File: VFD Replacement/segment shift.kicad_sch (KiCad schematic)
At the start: 28 parts, among them Q1 MMDT2222A

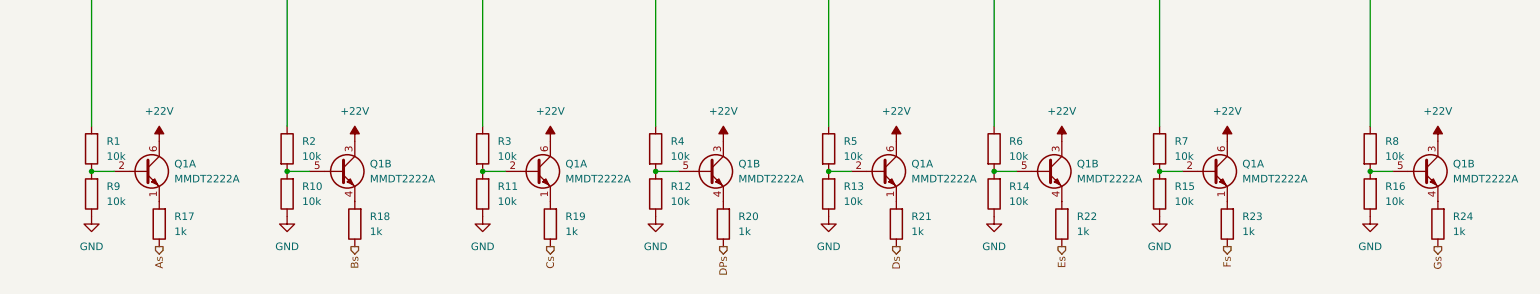
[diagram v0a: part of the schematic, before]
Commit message: Update VFD Replacement layout
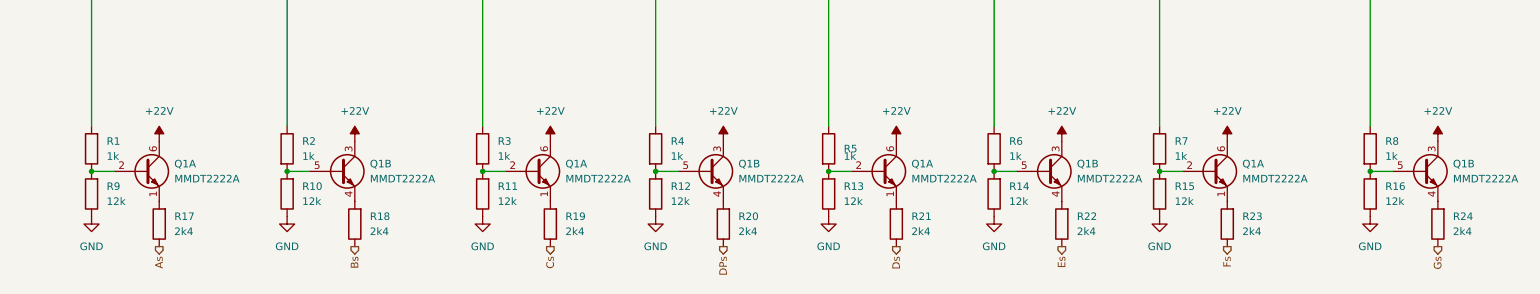
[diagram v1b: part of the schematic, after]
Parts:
- R1, R2, R3, R4, R5, R6, R7, R8: value 10k -> 1k
- R10, R11, R12, R13, R14, R15, R16, R9: value 10k -> 12k
- R17, R18, R19, R20, R21, R22, R23, R24: value 1k -> 2k4
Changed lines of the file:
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@@
       (effects (font (size 1.27 1.27)) (justify right))
     )
-    (property "Value" "10k" (at 132.08 120.6499 0)
+    (property "Value" "12k" (at 132.08 120.6499 0)
       (effects (font (size 1.27 1.27)) (justify right))
     )
@@
   (symbol (lib_id "Device:R") (at 158.75 111.76 0) (unit 1)
     (exclude_from_sim no) (in_bom yes) (on_board yes) (dnp no) (fields_autoplaced)
-    (property "Reference" "R5" (at 161.29 110.4899 0)
-      (effects (font (size 1.27 1.27)) (justify left))
-    )
-    (property "Value" "10k" (at 161.29 113.0299 0)
+    (property "Reference" "R5" (at 161.29 111.7599 0)
+      (effects (font (size 1.27 1.27)) (justify left))
+    )
+    (property "Value" "1k" (at 161.29 113.0299 0)
       (effects (font (size 1.27 1.27)) (justify left))
     )
@@
       (effects (font (size 1.27 1.27)) (justify left))
     )
-    (property "Value" "10k" (at 217.17 113.0299 0)
+    (property "Value" "1k" (at 217.17 113.0299 0)
       (effects (font (size 1.27 1.27)) (justify left))
     )
@@
       (effects (font (size 1.27 1.27)) (justify right))
     )
-    (property "Value" "1k" (at 228.6 125.7299 0)
+    (property "Value" "2k4" (at 228.6 125.7299 0)
       (effects (font (size 1.27 1.27)) (justify right))
     )
@@
       (effects (font (size 1.27 1.27)) (justify right))
     )
-    (property "Value" "1k" (at 172.72 125.7299 0)
+    (property "Value" "2k4" (at 172.72 125.7299 0)
       (effects (font (size 1.27 1.27)) (justify right))
     )
@@
       (effects (font (size 1.27 1.27)) (justify left))
     )
-    (property "Value" "10k" (at 132.08 113.0299 0)
+    (property "Value" "1k" (at 132.08 113.0299 0)
       (effects (font (size 1.27 1.27)) (justify left))
     )
@@
       (effects (font (size 1.27 1.27)) (justify right))
     )
-    (property "Value" "10k" (at 252.73 120.6499 0)
+    (property "Value" "12k" (at 252.73 120.6499 0)
       (effects (font (size 1.27 1.27)) (justify right))
     )
@@
       (effects (font (size 1.27 1.27)) (justify left))
     )
-    (property "Value" "10k" (at 189.23 113.0299 0)
+    (property "Value" "1k" (at 189.23 113.0299 0)
       (effects (font (size 1.27 1.27)) (justify left))
     )
@@
       (effects (font (size 1.27 1.27)) (justify right))
     )
-    (property "Value" "1k" (at 264.16 125.7299 0)
+    (property "Value" "2k4" (at 264.16 125.7299 0)
       (effects (font (size 1.27 1.27)) (justify right))
     )
@@
       (effects (font (size 1.27 1.27)) (justify right))
     )
-    (property "Value" "1k" (at 81.28 125.7299 0)
+    (property "Value" "2k4" (at 81.28 125.7299 0)
       (effects (font (size 1.27 1.27)) (justify right))
     )
@@
       (effects (font (size 1.27 1.27)) (justify right))
     )
-    (property "Value" "1k" (at 114.3 125.7299 0)
+    (property "Value" "2k4" (at 114.3 125.7299 0)
       (effects (font (size 1.27 1.27)) (justify right))
     )
@@
       (effects (font (size 1.27 1.27)) (justify right))
     )
-    (property "Value" "10k" (at 189.23 120.6499 0)
+    (property "Value" "12k" (at 189.23 120.6499 0)
       (effects (font (size 1.27 1.27)) (justify right))
     )
@@
       (effects (font (size 1.27 1.27)) (justify left))
     )
-    (property "Value" "10k" (at 69.85 113.0299 0)
+    (property "Value" "1k" (at 69.85 113.0299 0)
       (effects (font (size 1.27 1.27)) (justify left))
     )
@@
       (effects (font (size 1.27 1.27)) (justify right))
     )
-    (property "Value" "10k" (at 217.17 120.6499 0)
+    (property "Value" "12k" (at 217.17 120.6499 0)
       (effects (font (size 1.27 1.27)) (justify right))
     )
@@
       (effects (font (size 1.27 1.27)) (justify right))
     )
-    (property "Value" "1k" (at 143.51 125.7299 0)
+    (property "Value" "2k4" (at 143.51 125.7299 0)
       (effects (font (size 1.27 1.27)) (justify right))
     )
@@
       (effects (font (size 1.27 1.27)) (justify left))
     )
-    (property "Value" "10k" (at 102.87 113.0299 0)
+    (property "Value" "1k" (at 102.87 113.0299 0)
       (effects (font (size 1.27 1.27)) (justify left))
     )
@@
       (effects (font (size 1.27 1.27)) (justify left))
     )
-    (property "Value" "10k" (at 252.73 113.0299 0)
+    (property "Value" "1k" (at 252.73 113.0299 0)
       (effects (font (size 1.27 1.27)) (justify left))
     )
@@
       (effects (font (size 1.27 1.27)) (justify right))
     )
-    (property "Value" "1k" (at 48.26 125.7299 0)
+    (property "Value" "2k4" (at 48.26 125.7299 0)
       (effects (font (size 1.27 1.27)) (justify right))
     )
@@
       (effects (font (size 1.27 1.27)) (justify right))
     )
-    (property "Value" "10k" (at 69.85 120.6499 0)
+    (property "Value" "12k" (at 69.85 120.6499 0)
       (effects (font (size 1.27 1.27)) (justify right))
     )
@@
       (effects (font (size 1.27 1.27)) (justify right))
     )
-    (property "Value" "10k" (at 36.83 113.0299 0)
+    (property "Value" "1k" (at 36.83 113.0299 0)
       (effects (font (size 1.27 1.27)) (justify right))
     )
@@
       (effects (font (size 1.27 1.27)) (justify right))
     )
-    (property "Value" "10k" (at 161.29 120.6499 0)
+    (property "Value" "12k" (at 161.29 120.6499 0)
       (effects (font (size 1.27 1.27)) (justify right))
     )
@@
       (effects (font (size 1.27 1.27)) (justify right))
     )
-    (property "Value" "10k" (at 36.83 120.6499 0)
+    (property "Value" "12k" (at 36.83 120.6499 0)
       (effects (font (size 1.27 1.27)) (justify right))
     )
@@
       (effects (font (size 1.27 1.27)) (justify right))
     )
-    (property "Value" "1k" (at 200.66 125.7299 0)
+    (property "Value" "2k4" (at 200.66 125.7299 0)
       (effects (font (size 1.27 1.27)) (justify right))
     )
@@
       (effects (font (size 1.27 1.27)) (justify right))
     )
-    (property "Value" "10k" (at 102.87 120.6499 0)
-      (effects (font (size 1.27 1.27)) (justify right))
-    )
+    (property "Value" "12k" (at 102.87 120.6499 0)
+      (effects (font (size 1.27 1.27)) (justify right))
+    )

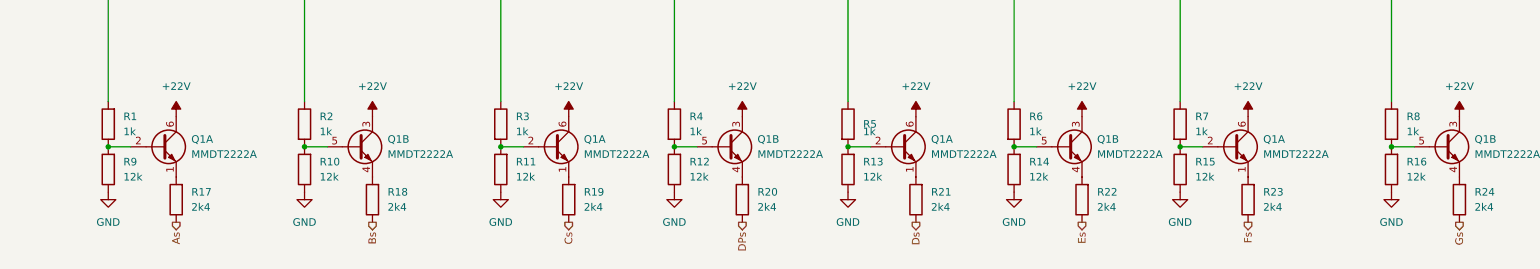
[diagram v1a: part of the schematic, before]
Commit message: Check 7-seg module and VFD interposer. Create outputs
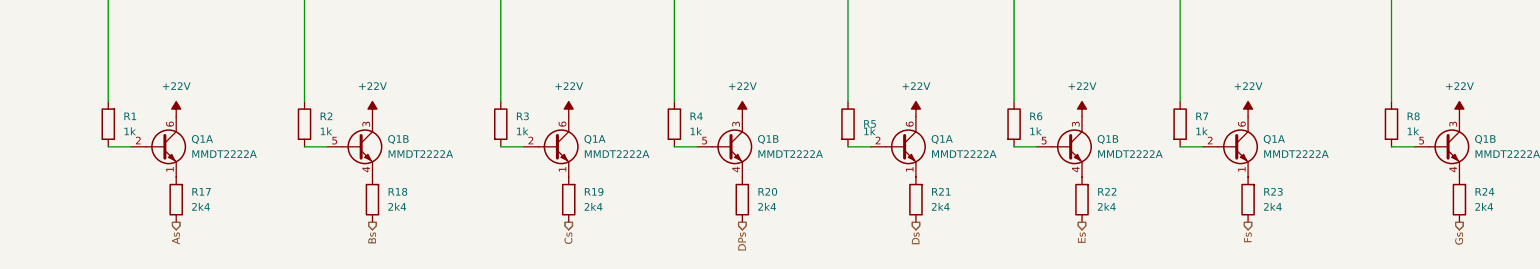
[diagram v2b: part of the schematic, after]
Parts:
- removed R10, R11, R12, R13, R14, R15, R16, R9: 12k, Resistor_SMD:R_0603_1608Metric_Pad0.98x0.95mm_HandSolder, symbol Device:R

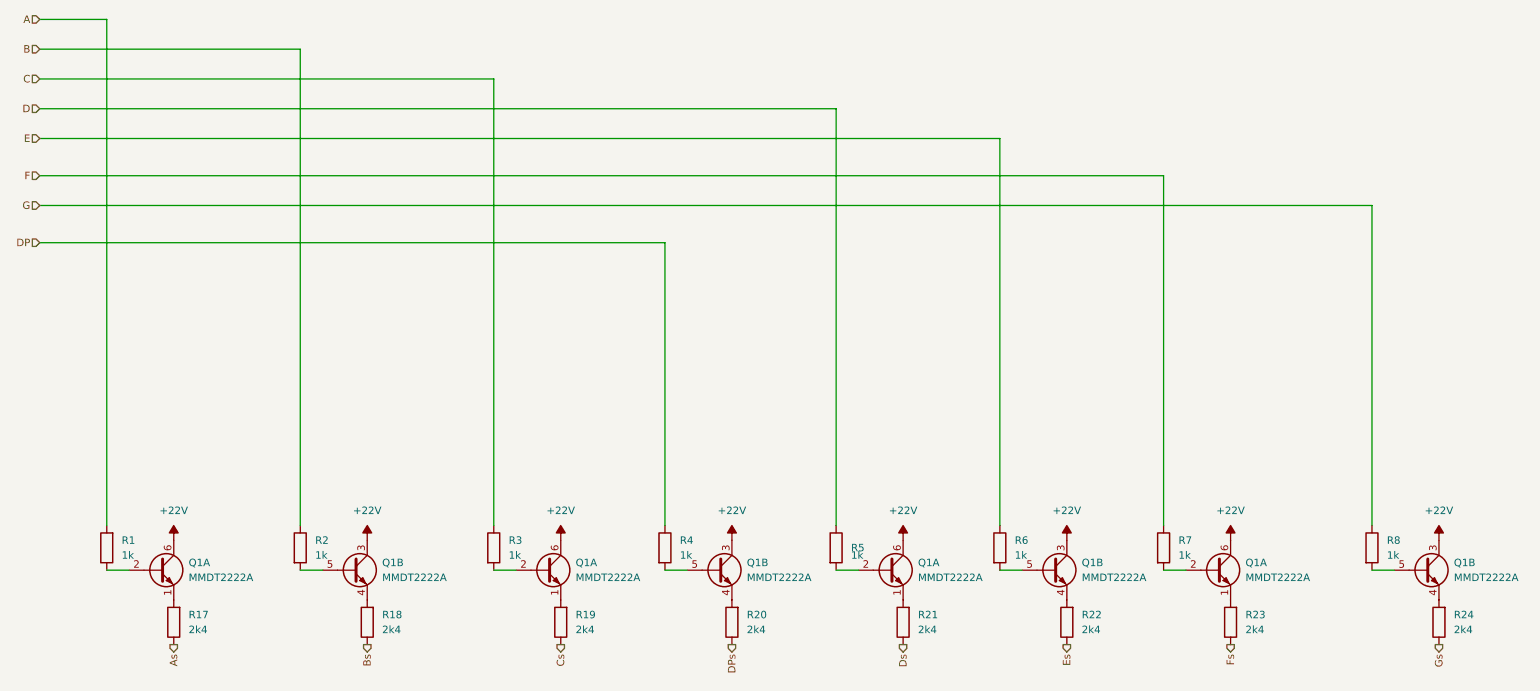
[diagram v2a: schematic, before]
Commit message: Update display base resistor values
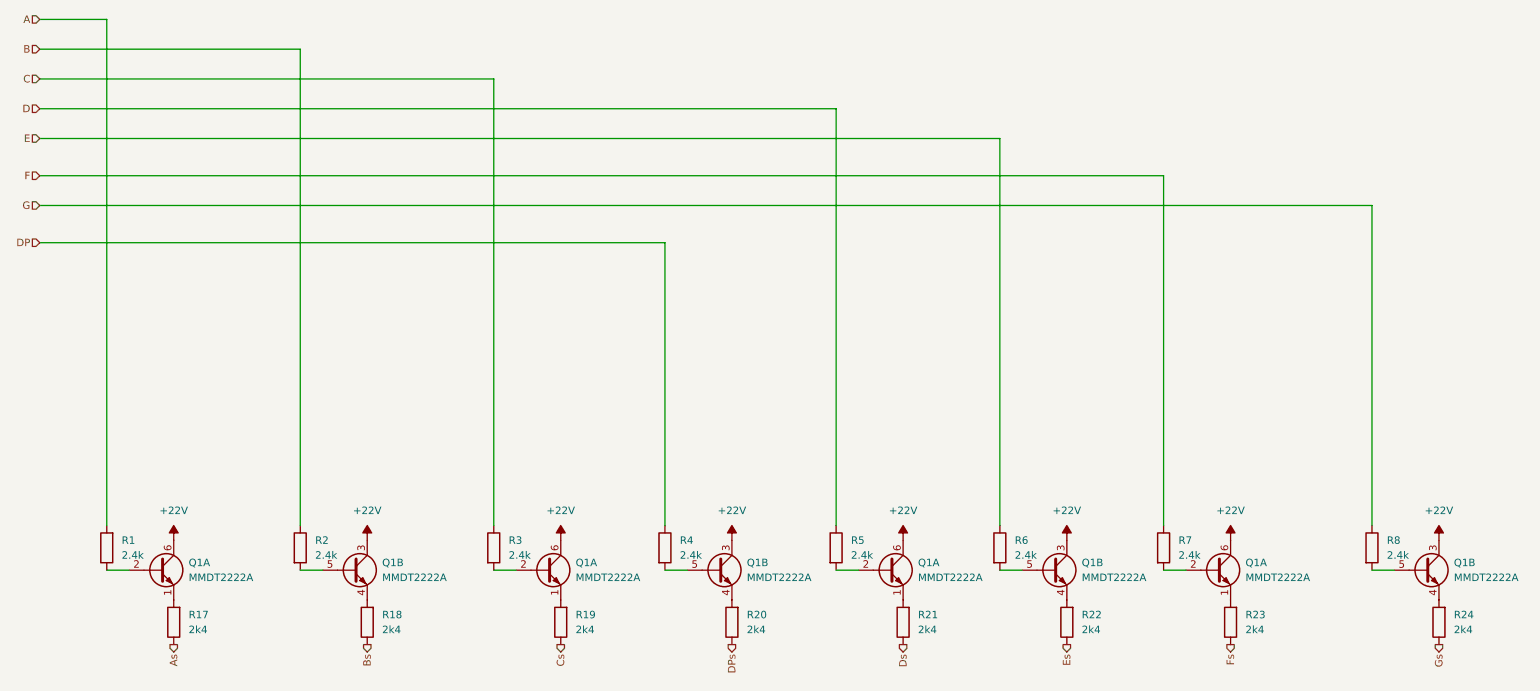
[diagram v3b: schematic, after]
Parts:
- R1, R2, R3, R4, R5, R6, R7, R8: value 1k -> 2.4k
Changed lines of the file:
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@@
   (symbol (lib_id "Device:R") (at 158.75 111.76 0) (unit 1)
     (exclude_from_sim no) (in_bom yes) (on_board yes) (dnp no) (fields_autoplaced)
-    (property "Reference" "R5" (at 161.29 111.7599 0)
-      (effects (font (size 1.27 1.27)) (justify left))
-    )
-    (property "Value" "1k" (at 161.29 113.0299 0)
+    (property "Reference" "R5" (at 161.29 110.4899 0)
+      (effects (font (size 1.27 1.27)) (justify left))
+    )
+    (property "Value" "2.4k" (at 161.29 113.0299 0)
       (effects (font (size 1.27 1.27)) (justify left))
     )
@@
       (effects (font (size 1.27 1.27)) (justify left))
     )
-    (property "Value" "1k" (at 217.17 113.0299 0)
+    (property "Value" "2.4k" (at 217.17 113.0299 0)
       (effects (font (size 1.27 1.27)) (justify left))
     )
@@
       (effects (font (size 1.27 1.27)) (justify left))
     )
-    (property "Value" "1k" (at 132.08 113.0299 0)
+    (property "Value" "2.4k" (at 132.08 113.0299 0)
       (effects (font (size 1.27 1.27)) (justify left))
     )
@@
       (effects (font (size 1.27 1.27)) (justify left))
     )
-    (property "Value" "1k" (at 189.23 113.0299 0)
+    (property "Value" "2.4k" (at 189.23 113.0299 0)
       (effects (font (size 1.27 1.27)) (justify left))
     )
@@
       (effects (font (size 1.27 1.27)) (justify left))
     )
-    (property "Value" "1k" (at 69.85 113.0299 0)
+    (property "Value" "2.4k" (at 69.85 113.0299 0)
       (effects (font (size 1.27 1.27)) (justify left))
     )
@@
       (effects (font (size 1.27 1.27)) (justify left))
     )
-    (property "Value" "1k" (at 102.87 113.0299 0)
+    (property "Value" "2.4k" (at 102.87 113.0299 0)
       (effects (font (size 1.27 1.27)) (justify left))
     )
@@
       (effects (font (size 1.27 1.27)) (justify left))
     )
-    (property "Value" "1k" (at 252.73 113.0299 0)
+    (property "Value" "2.4k" (at 252.73 113.0299 0)
       (effects (font (size 1.27 1.27)) (justify left))
     )
@@
       (effects (font (size 1.27 1.27)) (justify right))
     )
-    (property "Value" "1k" (at 36.83 113.0299 0)
-      (effects (font (size 1.27 1.27)) (justify right))
-    )
+    (property "Value" "2.4k" (at 36.83 113.0299 0)
+      (effects (font (size 1.27 1.27)) (justify right))
+    )

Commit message: Update values from sim
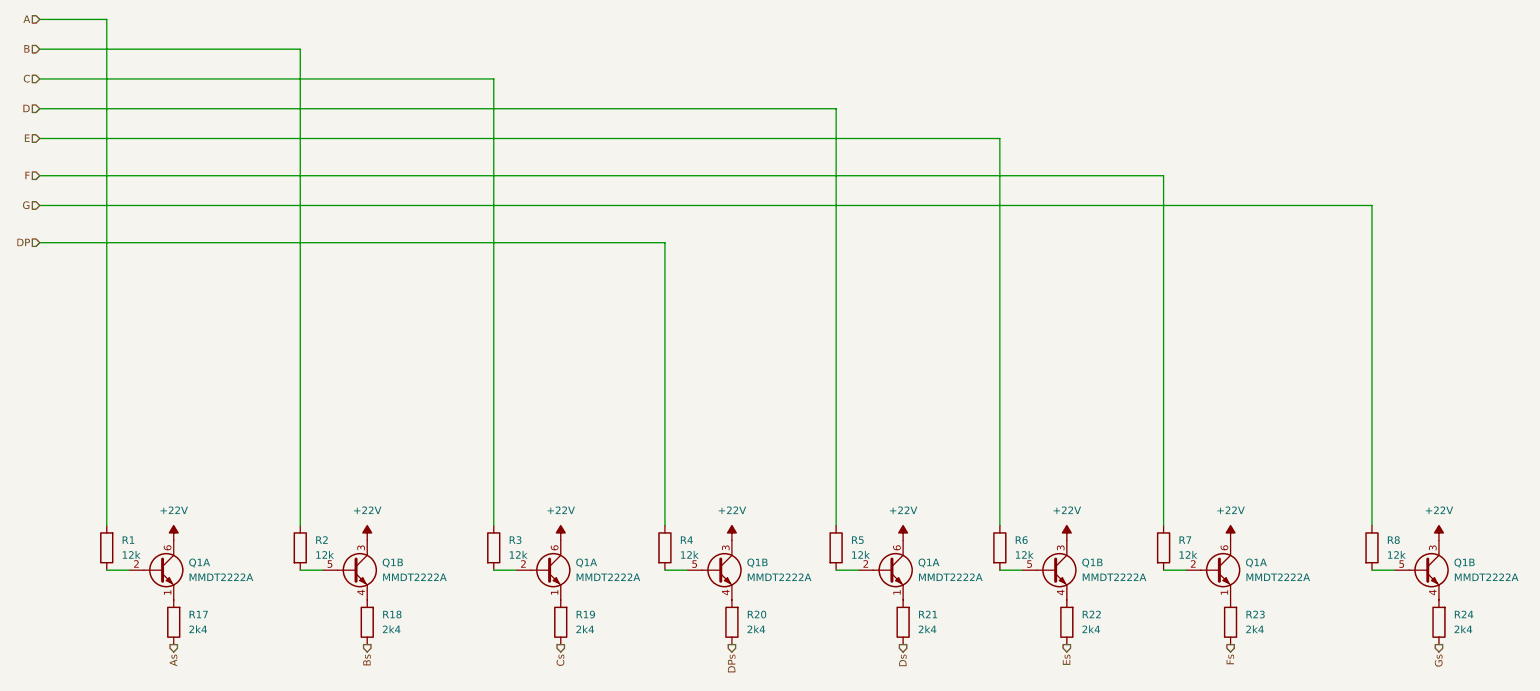
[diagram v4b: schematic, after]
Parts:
- R1, R2, R3, R4, R5, R6, R7, R8: value 2.4k -> 12k
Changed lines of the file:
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@@
       (effects (font (size 1.27 1.27)) (justify left))
     )
-    (property "Value" "2.4k" (at 161.29 113.0299 0)
+    (property "Value" "12k" (at 161.29 113.0299 0)
       (effects (font (size 1.27 1.27)) (justify left))
     )
@@
       (effects (font (size 1.27 1.27)) (justify left))
     )
-    (property "Value" "2.4k" (at 217.17 113.0299 0)
+    (property "Value" "12k" (at 217.17 113.0299 0)
       (effects (font (size 1.27 1.27)) (justify left))
     )
@@
       (effects (font (size 1.27 1.27)) (justify left))
     )
-    (property "Value" "2.4k" (at 132.08 113.0299 0)
+    (property "Value" "12k" (at 132.08 113.0299 0)
       (effects (font (size 1.27 1.27)) (justify left))
     )
@@
       (effects (font (size 1.27 1.27)) (justify left))
     )
-    (property "Value" "2.4k" (at 189.23 113.0299 0)
+    (property "Value" "12k" (at 189.23 113.0299 0)
       (effects (font (size 1.27 1.27)) (justify left))
     )
@@
       (effects (font (size 1.27 1.27)) (justify left))
     )
-    (property "Value" "2.4k" (at 69.85 113.0299 0)
+    (property "Value" "12k" (at 69.85 113.0299 0)
       (effects (font (size 1.27 1.27)) (justify left))
     )
@@
       (effects (font (size 1.27 1.27)) (justify left))
     )
-    (property "Value" "2.4k" (at 102.87 113.0299 0)
+    (property "Value" "12k" (at 102.87 113.0299 0)
       (effects (font (size 1.27 1.27)) (justify left))
     )
@@
       (effects (font (size 1.27 1.27)) (justify left))
     )
-    (property "Value" "2.4k" (at 252.73 113.0299 0)
+    (property "Value" "12k" (at 252.73 113.0299 0)
       (effects (font (size 1.27 1.27)) (justify left))
     )
@@
       (effects (font (size 1.27 1.27)) (justify right))
     )
-    (property "Value" "2.4k" (at 36.83 113.0299 0)
-      (effects (font (size 1.27 1.27)) (justify right))
-    )
+    (property "Value" "12k" (at 36.83 113.0299 0)
+      (effects (font (size 1.27 1.27)) (justify right))
+    )
